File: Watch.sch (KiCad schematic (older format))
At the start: 11 parts

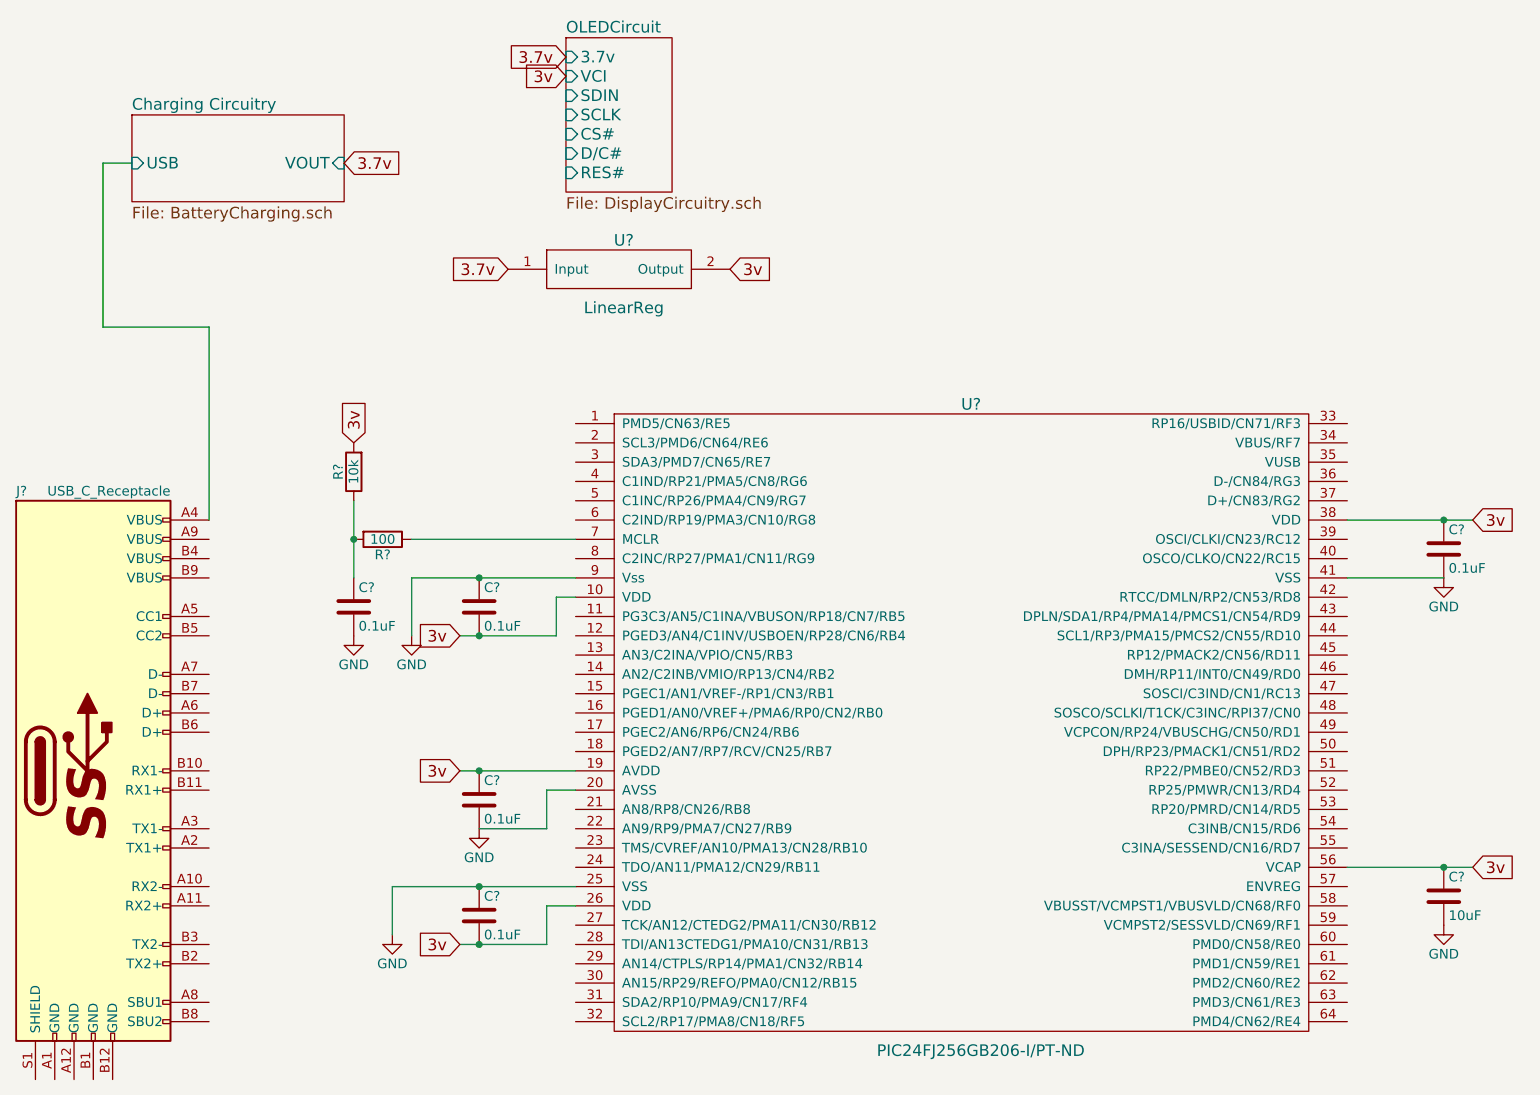
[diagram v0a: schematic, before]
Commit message: added SPI connections for OLED
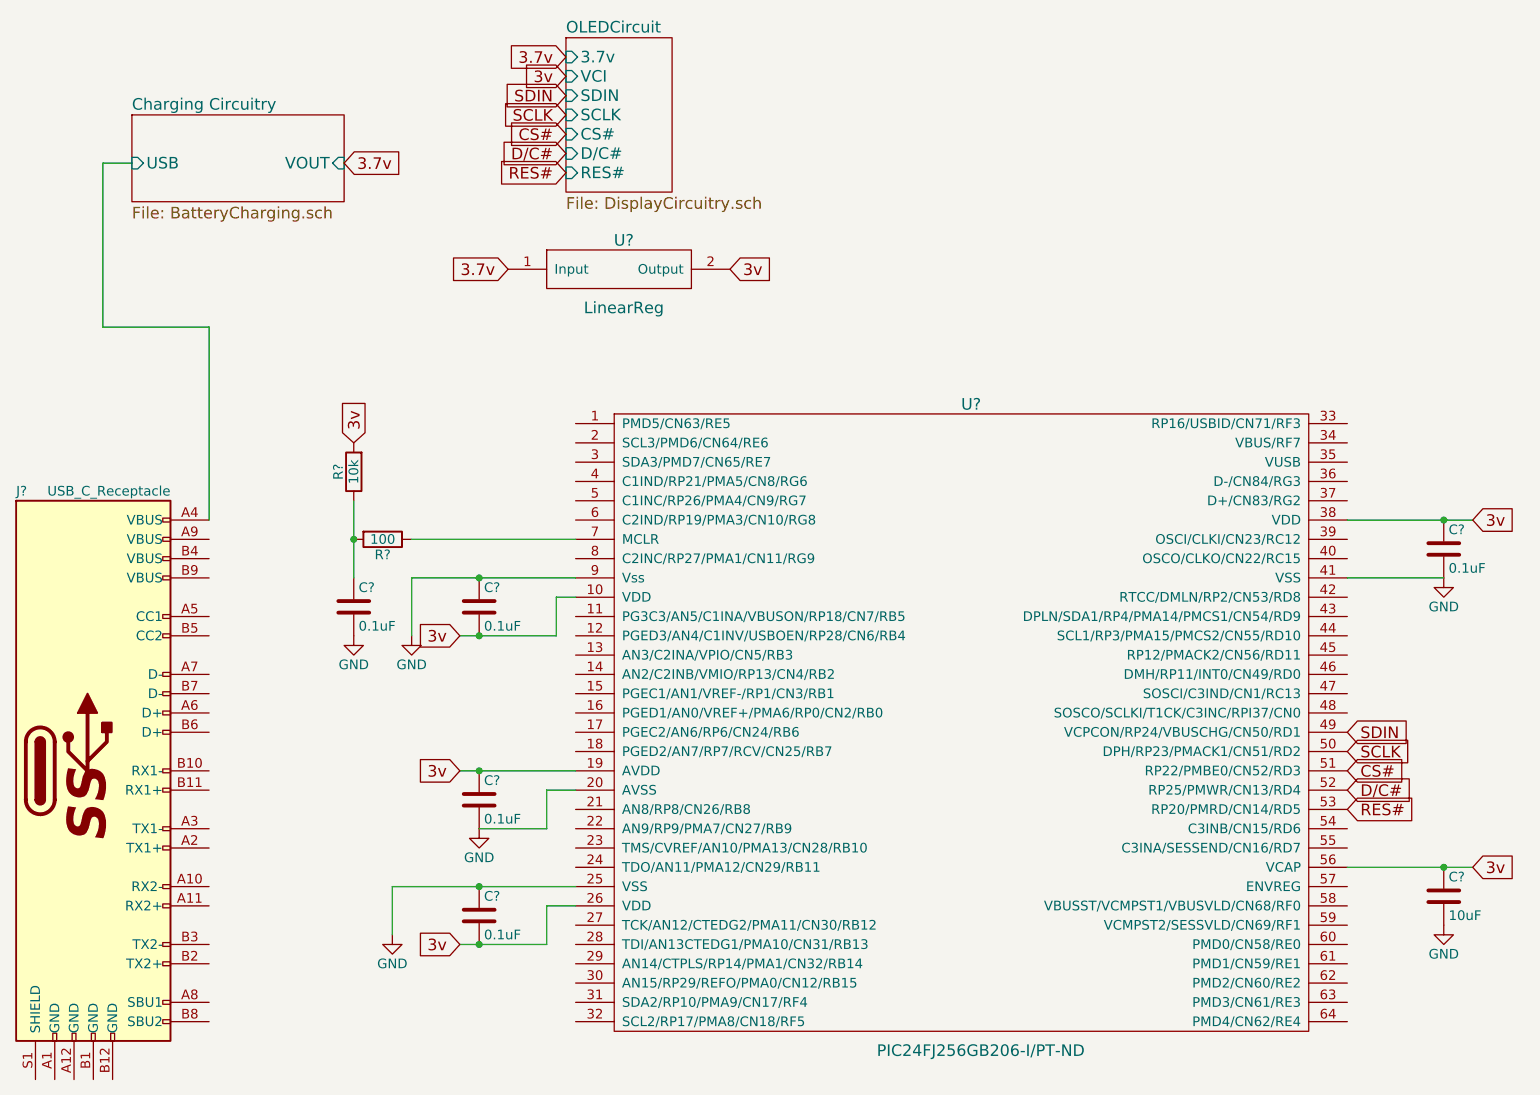
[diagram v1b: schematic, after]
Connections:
- net SDIN: now reaches U?.49 (VCPCON/RP24/VBUSCHG/CN50/RD1)
- net SCLK: now reaches U?.50 (DPH/RP23/PMACK1/CN51/RD2)
- net CS#: now reaches U?.51 (RP22/PMBE0/CN52/RD3)
- net D/C#: now reaches U?.52 (RP25/PMWR/CN13/RD4)
- net RES#: now reaches U?.53 (RP20/PMRD/CN14/RD5)
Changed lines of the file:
@@
 Text GLabel 3550 1150 0    60   Input ~ 0
 3v
+Text GLabel 7600 4950 2    60   Input ~ 0
+RES#
+Text GLabel 7600 4850 2    60   Input ~ 0
+D/C#
+Text GLabel 7600 4750 2    60   Input ~ 0
+CS#
+Text GLabel 7600 4650 2    60   Input ~ 0
+SCLK
+Text GLabel 7600 4550 2    60   Input ~ 0
+SDIN
+Text GLabel 3550 1250 0    60   Input ~ 0
+SDIN
+Text GLabel 3550 1350 0    60   Input ~ 0
+SCLK
+Text GLabel 3550 1450 0    60   Input ~ 0
+CS#
+Text GLabel 3550 1550 0    60   Input ~ 0
+D/C#
+Text GLabel 3550 1650 0    60   Input ~ 0
+RES#
 $EndSCHEMATC
